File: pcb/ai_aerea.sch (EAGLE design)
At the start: 26 parts, among them J1 JST-2-MALE, J2 1X02ST, U1 MCP73831

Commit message: routing
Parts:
- added STANDOFF1, STANDOFF2, STANDOFF3, STANDOFF4: STAND-OFF, Ai_Electromechanical:STAND-OFF
- added U$3: AI-LOGOXS, Ai_Miscellany:AI-LOGOXS
- C1, C2, C3, C4: device Ai_Passives:CAP0603 -> Ai_Passives:CAP025X050
- D1: device Ai_DiscreteSemis:DIODESMA-403D -> Ai_DiscreteSemis:DIODETH-1N914
- LED1, LED2, LED3, LED4, LED5, LED6: device Ai_LED:LED0805 -> Ai_LED:LED5MM
- R1, R3, R4, R5, R6, R7: device Ai_Passives:RES0603 -> Ai_Passives:RESAXIAL-0.4
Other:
- moved on the sheet: C1, C2, C3, C4, D1, J1, J2, LED1, LED2, LED3, LED4, LED5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

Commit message: gerbers generated
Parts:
- removed U$3: AI-LOGOXS, Ai_Miscellany:AI-LOGOXS
- added U$4: AI-LOGOM, Ai_Miscellany:AI-LOGOM
- renumbered R2 to LDR, VR1 to BRT
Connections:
- net N$1 renamed VPANEL
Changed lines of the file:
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@@
 <part name="R1" library="Ai_Passives" deviceset="RES" device="AXIAL-0.4" value="2K"/>
 <part name="GND2" library="Ai_Power" deviceset="GND" device=""/>
-<part name="R2" library="Ai_Sensors" deviceset="LDR" device="-PTH"/>
-<part name="VR1" library="Ai_Passives" deviceset="POT" device="05X05"/>
+<part name="LDR" library="Ai_Sensors" deviceset="LDR" device="-PTH"/>
+<part name="BRT" library="Ai_Passives" deviceset="POT" device="05X05"/>
 <part name="LED1" library="Ai_LED" deviceset="LED" device="5MM"/>
 <part name="LED2" library="Ai_LED" deviceset="LED" device="5MM"/>
@@
 <part name="U$1" library="Ai_Power" deviceset="VBAT" device=""/>
 <part name="U$2" library="Ai_Power" deviceset="VBAT" device=""/>
-<part name="U$3" library="Ai_Miscellany" deviceset="AI-LOGO" device="XS"/>
+<part name="U$4" library="Ai_Miscellany" deviceset="AI-LOGO" device="M" value="AI-LOGOM"/>
 <part name="STANDOFF1" library="Ai_Electromechanical" deviceset="STAND-OFF" device=""/>
 <part name="STANDOFF2" library="Ai_Electromechanical" deviceset="STAND-OFF" device=""/>
@@
 <instance part="R1" gate="G$1" x="106.68" y="123.19" rot="R90"/>
 <instance part="GND2" gate="GND" x="111.76" y="110.49"/>
-<instance part="R2" gate="G$1" x="76.2" y="55.88" rot="R90"/>
-<instance part="VR1" gate="G$1" x="110.49" y="55.88" rot="R180"/>
+<instance part="LDR" gate="G$1" x="76.2" y="55.88" rot="R90"/>
+<instance part="BRT" gate="G$1" x="110.49" y="55.88" rot="R180"/>
 <instance part="LED1" gate="G$1" x="142.24" y="78.74"/>
 <instance part="LED2" gate="G$1" x="148.59" y="78.74"/>
@@
 <instance part="U$1" gate="G$1" x="106.68" y="133.35"/>
 <instance part="U$2" gate="G$1" x="76.2" y="90.17"/>
-<instance part="U$3" gate="G$1" x="130.81" y="24.13"/>
+<instance part="U$4" gate="G$1" x="130.81" y="24.13"/>
 <instance part="STANDOFF1" gate="G$1" x="135.89" y="11.43"/>
 <instance part="STANDOFF2" gate="G$1" x="128.27" y="11.43"/>
@@
 </busses>
 <nets>
-<net name="N$1" class="0">
+<net name="VPANEL" class="0">
 <segment>
 <pinref part="J2" gate="G$1" pin="2"/>
 <pinref part="D1" gate="G$1" pin="A"/>
-<wire x1="62.23" y1="130.81" x2="64.77" y2="130.81" width="0.1524" layer="91"/>
+<wire x1="62.23" y1="130.81" x2="63.5" y2="130.81" width="0.1524" layer="91"/>
+<wire x1="63.5" y1="130.81" x2="64.77" y2="130.81" width="0.1524" layer="91"/>
+<wire x1="63.5" y1="130.81" x2="63.5" y2="133.35" width="0.1524" layer="91"/>
+<junction x="63.5" y="130.81"/>
+<label x="63.5" y="133.35" size="1.27" layer="95" font="vector" ratio="10" rot="R90" xref="yes"/>
 </segment>
 </net>
@@
 </segment>
 <segment>
-<pinref part="R2" gate="G$1" pin="P$1"/>
+<pinref part="LDR" gate="G$1" pin="P$1"/>
 <wire x1="76.2" y1="48.26" x2="76.2" y2="46.99" width="0.1524" layer="91"/>
 <wire x1="76.2" y1="46.99" x2="83.82" y2="46.99" width="0.1524" layer="91"/>
@@
 <pinref part="GND5" gate="GND" pin="GND"/>
 <wire x1="83.82" y1="46.99" x2="83.82" y2="44.45" width="0.1524" layer="91"/>
-<pinref part="VR1" gate="G$1" pin="E"/>
+<pinref part="BRT" gate="G$1" pin="E"/>
 <wire x1="110.49" y1="46.99" x2="110.49" y2="50.8" width="0.1524" layer="91"/>
 </segment>
@@
 <wire x1="76.2" y1="87.63" x2="105.41" y2="87.63" width="0.1524" layer="91"/>
 <wire x1="105.41" y1="87.63" x2="105.41" y2="85.09" width="0.1524" layer="91"/>
-<pinref part="VR1" gate="G$1" pin="A"/>
+<pinref part="BRT" gate="G$1" pin="A"/>
 <wire x1="105.41" y1="87.63" x2="110.49" y2="87.63" width="0.1524" layer="91"/>
 <wire x1="110.49" y1="87.63" x2="110.49" y2="60.96" width="0.1524" layer="91"/>
@@
 <net name="N$10" class="0">
 <segment>
-<pinref part="R2" gate="G$1" pin="P$2"/>
+<pinref part="LDR" gate="G$1" pin="P$2"/>
 <pinref part="R5" gate="G$1" pin="1"/>
 <wire x1="76.2" y1="63.5" x2="76.2" y2="64.77" width="0.1524" layer="91"/>
@@
 <net name="-" class="0">
 <segment>
-<pinref part="VR1" gate="G$1" pin="S"/>
+<pinref part="BRT" gate="G$1" pin="S"/>
 <pinref part="R7" gate="G$1" pin="1"/>
 <wire x1="105.41" y1="64.77" x2="100.33" y2="64.77" width="0.1524" layer="91"/>

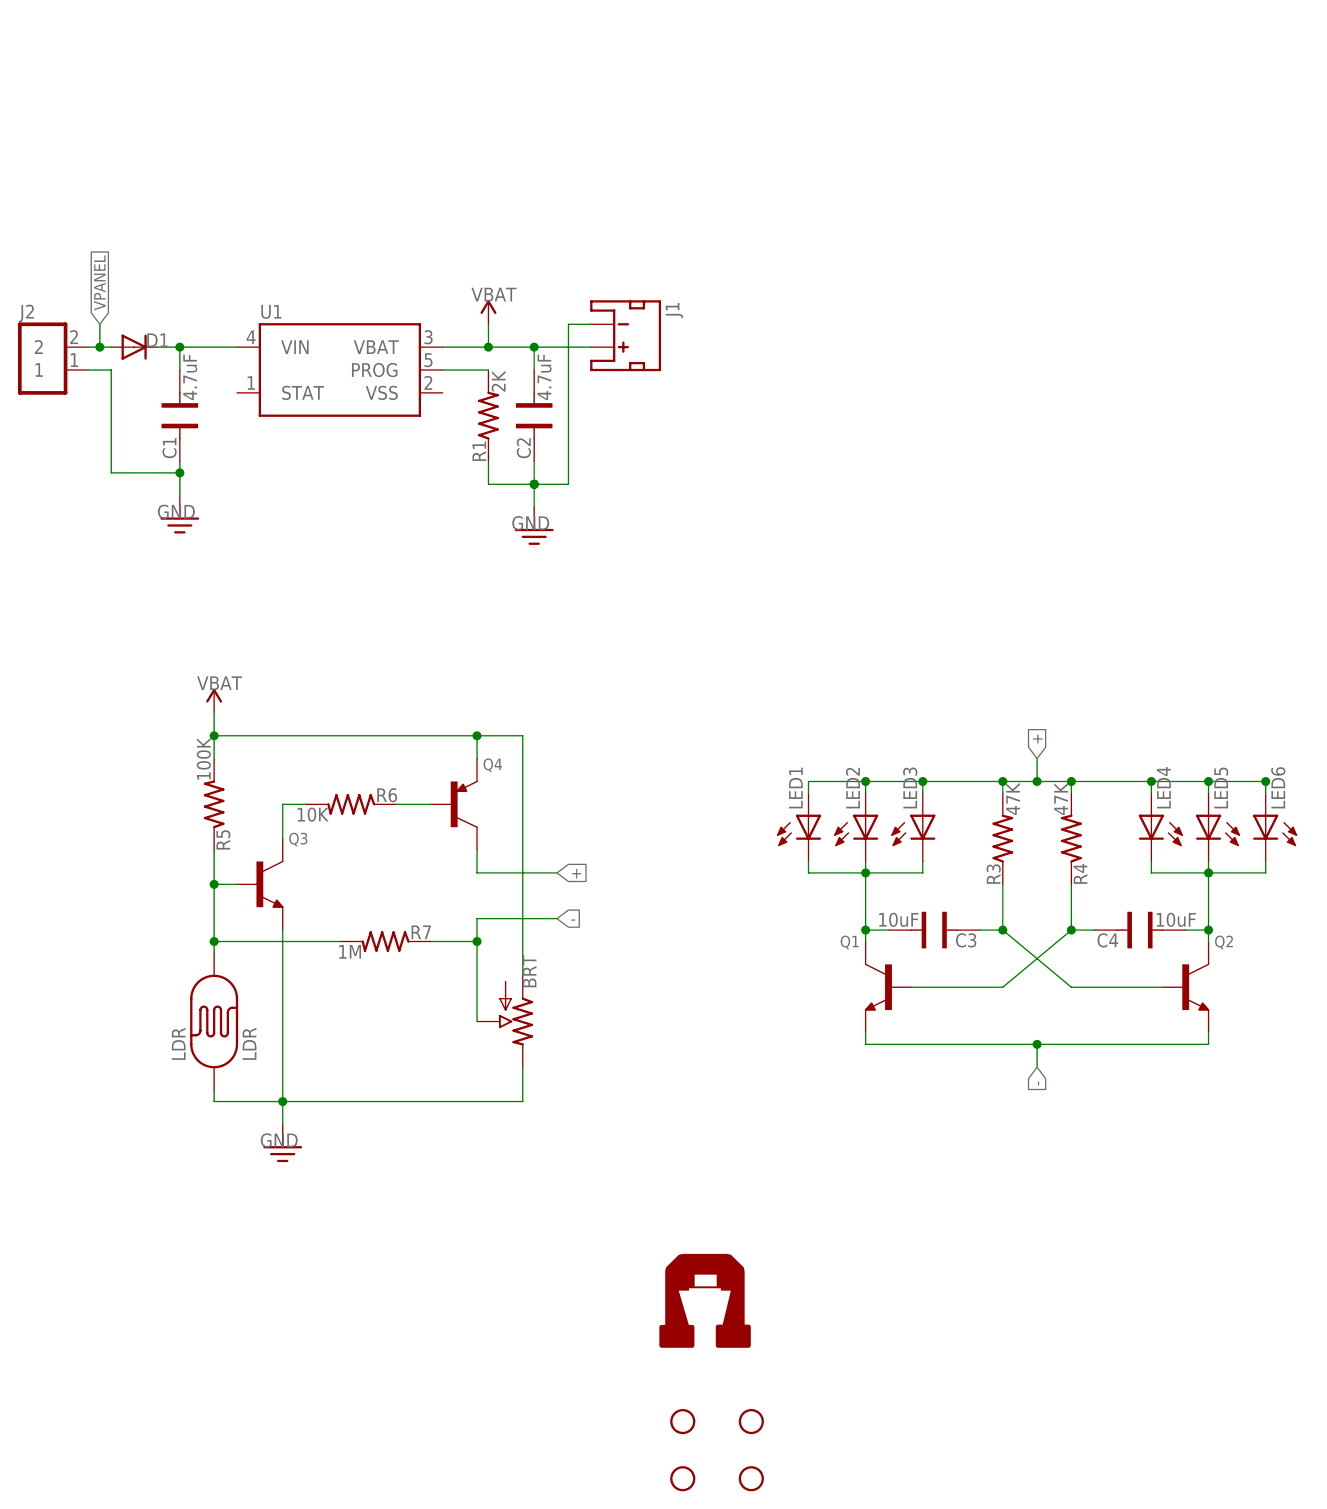
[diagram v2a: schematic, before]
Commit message: going with a square design
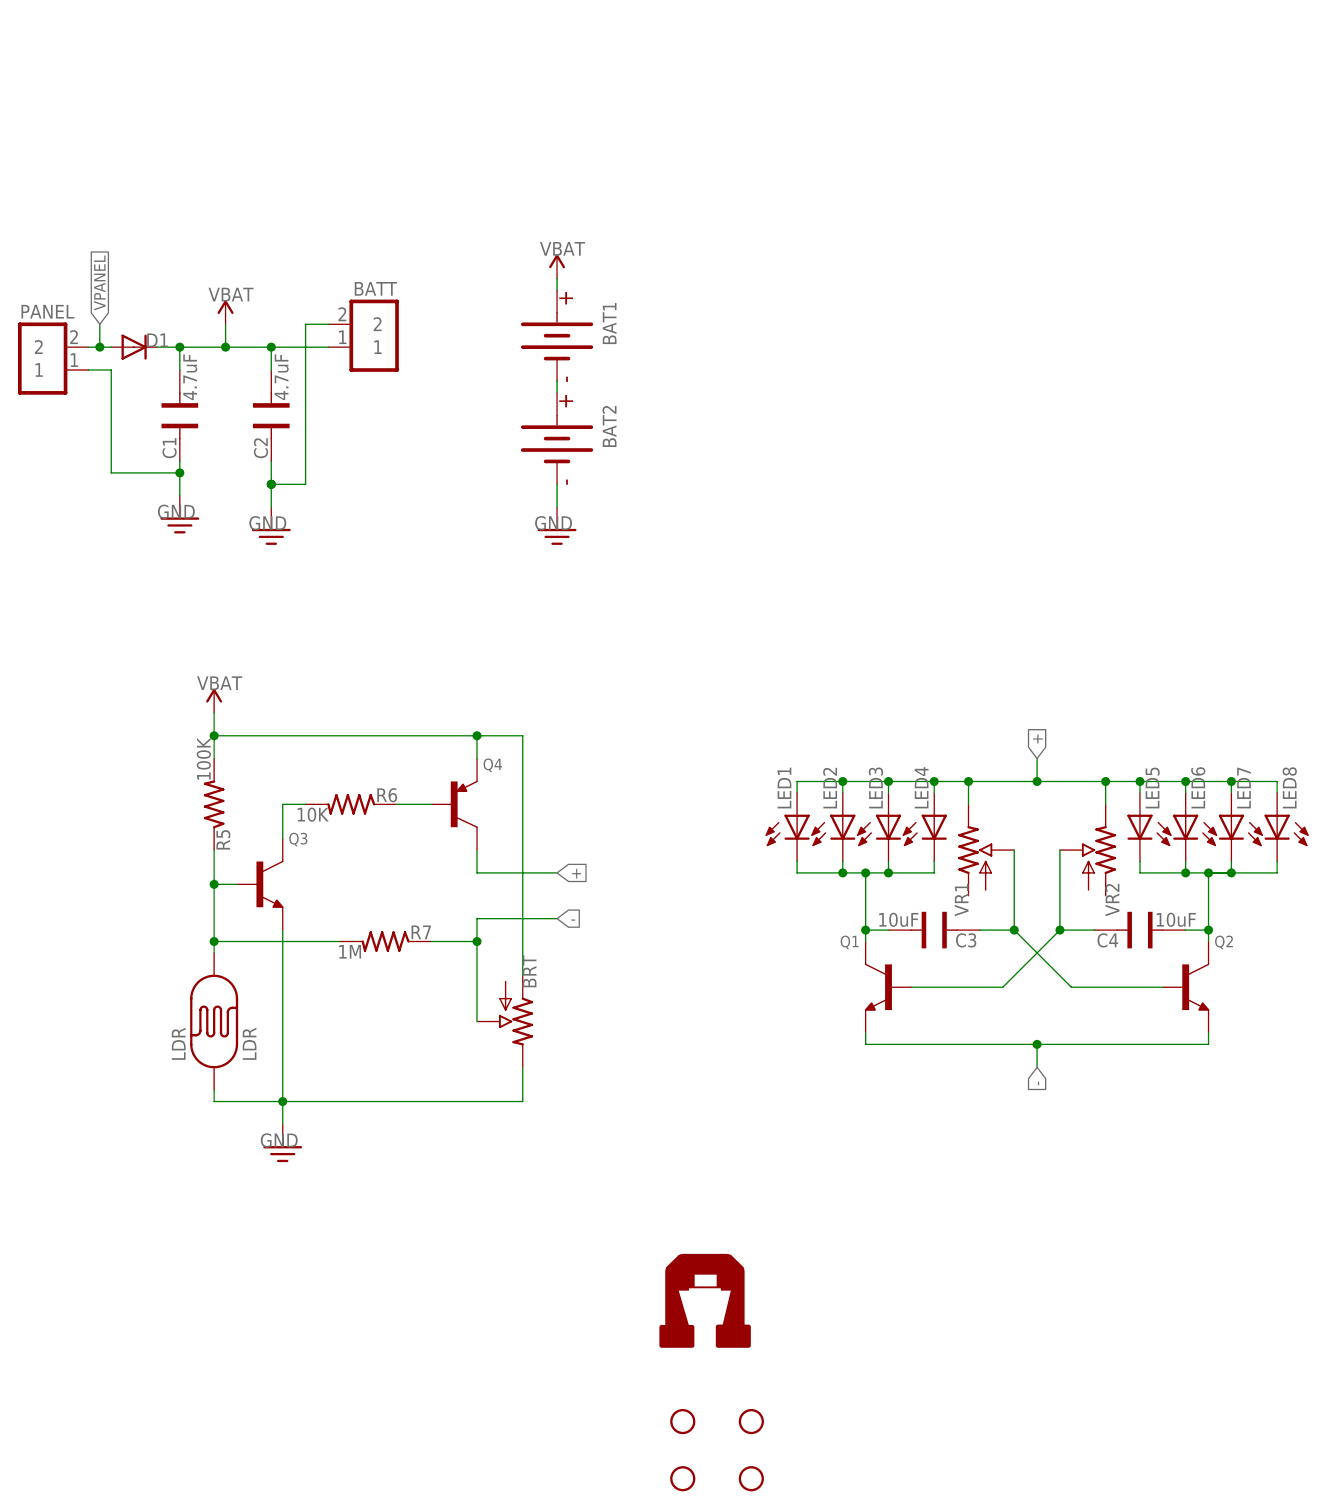
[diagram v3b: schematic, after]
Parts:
- removed J1: JST-2-MALE, Ai_Connectors:JST-2-MALE
- removed R1: 2K, Ai_Passives:RESAXIAL-0.4
- removed R3, R4: 47K, Ai_Passives:RESAXIAL-0.4
- removed U1: MCP73831, Ai_IC:MCP73831
- added BAT1, BAT2: (no value), Ai_Electromechanical:BATTERY-HOLDER
- added BATT: 1X02ST, Ai_Connectors:1X02ST
- added LED7, LED8: (no value), Ai_LED:LED5MM
- added VR1, VR2: (no value), Ai_Passives:POT05X05
- renumbered J2 to PANEL
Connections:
- removed net N$2: C1.1, D1.C, U1.VIN
- removed net N$9: C4.1, LED4.C, LED5.C, LED6.C, Q2.C
- new net N$1: BAT1.-, BAT2.+
- net +: now also LED7.A, LED8.A, VR1.E, VR2.E; no longer R3.2, R4.2
- net GND: now also BAT2.-, BATT.2; no longer J1.-, R1.1
- net N$14: now also LED4.C
- net N$3: now also C4.1, LED5.C, LED6.C, LED7.C, LED8.C, Q2.C; no longer R1.2, U1.PROG
- net N$6: now also VR1.S; no longer R3.1
- net N$7: now also VR2.S; no longer R4.1
- net VBAT: now also BAT1.+, BATT.1, C1.1, D1.C; no longer J1.+, U1.VBAT
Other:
- moved on the sheet: C2, LED1, LED2, LED3, LED4, LED5, LED6
